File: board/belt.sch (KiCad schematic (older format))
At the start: 21 parts, among them J1 USB_B_Micro, J2 USB_B_Micro, J3 USB_B_Micro, J4 USB_B_Micro, Q1 BSS138, Q2 BSS138, SW1 SW_SPST, SW2 SW_Push, U1 Teensy4.0, U2 Adafruit_BNO055

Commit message: first pass at pcb layout; also start looking into adding an NPN switch so that LED current doesn't have to travel through the rest of the board (concerns about wire thickness, heat, etc.)
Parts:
- added Q3: TIP120, Package_TO_SOT_THT:TO-220-3_Vertical, symbol Transistor_BJT:TIP120
- added R5: 5K, Resistor_SMD:R_0805_2012Metric, symbol Device:R_Small_US
- MK1: symbol SPW2430HR5H-B:SPW2430HR5H-B -> MIC_SPW2430HR5H-B:SPW2430HR5H-B
- R5: symbol 3352T-1-103LF:3352T-1-103LF -> belt-rescue:3352T-1-103LF-3352T-1-103LF
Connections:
- net labels added: GND_SWITCH
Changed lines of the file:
@@
-	1    0    0    -1
-$EndComp
-$Comp
-L power:GND #PWR0116
-U 1 1 5E3355B9
-P 4000 5700
-F 0 "#PWR0116" H 4000 5450 50  0001 C CNN
-F 1 "GND" V 4005 5572 50  0000 R CNN
-F 2 "" H 4000 5700 50  0001 C CNN
-F 3 "" H 4000 5700 50  0001 C CNN
-	1    4000 5700
 	1    0    0    -1
 $EndComp
 Connection ~ 3000 5600
-Wire Wire Line
-	2700 5600 3000 5600
 $Comp
 L Device:C C1
@@
 	3450 7150 3450 6950
 $Comp
-L SPW2430HR5H-B:SPW2430HR5H-B MK1
+L MIC_SPW2430HR5H-B:SPW2430HR5H-B MK1
 U 1 1 5E34E597
 P 3250 6450
@@
 BUTTON
 $Comp
-L 3352T-1-103LF:3352T-1-103LF R5
+L belt-rescue:3352T-1-103LF-3352T-1-103LF R5
 U 1 1 5E3B3B17
 P 1500 1050
@@
 	0    1    1    0
 $EndComp
-$Comp
-L power:VDD #PWR0123
-U 1 1 5E3B5DE6
-P 1800 1050
-F 0 "#PWR0123" H 1800 900 50  0001 C CNN
-F 1 "VDD" V 1817 1178 50  0000 L CNN
-F 2 "" H 1800 1050 50  0001 C CNN
-F 3 "" H 1800 1050 50  0001 C CNN
-	1    1800 1050
-	0    1    1    0
-$EndComp
 Text Label 6650 950  1    50   ~ 0
 THUMBDIAL
@@
 Text Label 6450 3150 3    50   ~ 0
 MOTION_SCL
-$Comp
-L power:GND #PWR0112
-U 1 1 5E31B962
-P 4000 4500
-F 0 "#PWR0112" H 4000 4250 50  0001 C CNN
-F 1 "GND" V 4005 4372 50  0000 R CNN
-F 2 "" H 4000 4500 50  0001 C CNN
-F 3 "" H 4000 4500 50  0001 C CNN
-	1    4000 4500
-	1    0    0    -1
-$EndComp
 $Comp
 L power:VDD #PWR02
@@
 Connection ~ 3650 5600
 $Comp
-L power:GND #PWR0129
-U 1 1 5E37E624
-P 4300 4900
-F 0 "#PWR0129" H 4300 4650 50  0001 C CNN
-F 1 "GND" V 4305 4772 50  0000 R CNN
-F 2 "" H 4300 4900 50  0001 C CNN
-F 3 "" H 4300 4900 50  0001 C CNN
-	1    4300 4900
-	0    1    1    0
-$EndComp
-$Comp
 L power:VDD #PWR0130
 U 1 1 5E37EDC1
@@
 $EndComp
 $Comp
-L power:GND #PWR0131
-U 1 1 5E3831AA
-P 4300 6100
-F 0 "#PWR0131" H 4300 5850 50  0001 C CNN
-F 1 "GND" V 4305 5972 50  0000 R CNN
-F 2 "" H 4300 6100 50  0001 C CNN
-F 3 "" H 4300 6100 50  0001 C CNN
-	1    4300 6100
-	0    1    1    0
-$EndComp
-$Comp
 L power:VDD #PWR0132
 U 1 1 5E3831B0
@@
 NoConn ~ 2750 1200
 NoConn ~ 2850 1200
+$Comp
+L power:+3.3V #PWR0123
+U 1 1 5E3638F7
+P 1800 1050
+F 0 "#PWR0123" H 1800 900 50  0001 C CNN
+F 1 "+3.3V" V 1815 1178 50  0000 L CNN
+F 2 "" H 1800 1050 50  0001 C CNN
+F 3 "" H 1800 1050 50  0001 C CNN
+	1    1800 1050
+	0    1    1    0
+$EndComp
+Wire Wire Line
+	2700 5600 3000 5600
+Text Label 2850 3250 0    50   ~ 0
+GND_SWITCH
+Text Label 4300 6100 2    50   ~ 0
+GND_SWITCH
+Text Label 4000 5700 2    50   ~ 0
+GND_SWITCH
+Text Label 4300 4900 2    50   ~ 0
+GND_SWITCH
+Text Label 4000 4500 2    50   ~ 0
+GND_SWITCH
+$Comp
+L Transistor_BJT:TIP120 Q3
+U 1 1 5E42DE1B
+P 2650 3150
+F 0 "Q3" V 2901 3150 50  0000 C CNN
+F 1 "TIP120" V 2992 3150 50  0000 C CNN
+F 2 "Package_TO_SOT_THT:TO-220-3_Vertical" H 2850 3075 50  0001 L CIN
+F 3 "http://www.fairchildsemi.com/ds/TI/TIP120.pdf" H 2650 3150 50  0001 L CNN
+	1    2650 3150
+	0    1    1    0
+$EndComp
+$Comp
+L power:GND #PWR?
+U 1 1 5E433994
+P 2450 3250
+F 0 "#PWR?" H 2450 3000 50  0001 C CNN
+F 1 "GND" V 2455 3122 50  0000 R CNN
+F 2 "" H 2450 3250 50  0001 C CNN
+F 3 "" H 2450 3250 50  0001 C CNN
+	1    2450 3250
+	0    1    1    0
+$EndComp
+$Comp
+L power:VDD #PWR?
+U 1 1 5E434E74
+P 2650 2750
+F 0 "#PWR?" H 2650 2600 50  0001 C CNN
+F 1 "VDD" V 2667 2878 50  0000 L CNN
+F 2 "" H 2650 2750 50  0001 C CNN
+F 3 "" H 2650 2750 50  0001 C CNN
+	1    2650 2750
+	1    0    0    -1
+$EndComp
+$Comp
+L Device:R_Small_US R5
+U 1 1 5E43706E
+P 2650 2850
+F 0 "R5" H 2718 2896 50  0000 L CNN
+F 1 "5K" H 2718 2805 50  0000 L CNN
+F 2 "Resistor_SMD:R_0805_2012Metric" H 2650 2850 50  0001 C CNN
+F 3 "~" H 2650 2850 50  0001 C CNN
+	1    2650 2850
+	1    0    0    -1
+$EndComp
 $EndSCHEMATC

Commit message: alternate layout with thick wires and switch on top to avoid needing a transistor to switch power nearby (would likely need a large transistor with a heatsink to manage the current)
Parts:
- removed Q3: TIP120, Package_TO_SOT_THT:TO-220-3_Vertical, symbol Transistor_BJT:TIP120
- removed R5: 5K, Resistor_SMD:R_0805_2012Metric, symbol Device:R_Small_US
- renumbered R5 to P1
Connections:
- net labels added: MIC_PWR
- net labels removed: GND_SWITCH
- no-connect marks 64 -> 63
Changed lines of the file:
@@
-	0    1    1    0
-$EndComp
-$Comp
-L power:+3.3V #PWR0114
-U 1 1 5E354D35
-P 3600 7150
-F 0 "#PWR0114" H 3600 7000 50  0001 C CNN
-F 1 "+3.3V" V 3615 7278 50  0000 L CNN
-F 2 "" H 3600 7150 50  0001 C CNN
-F 3 "" H 3600 7150 50  0001 C CNN
-	1    3600 7150
 	0    1    1    0
 $EndComp
@@
 Text Label 2700 5600 2    50   ~ 0
 DATA2
-NoConn ~ 6450 950
 $Comp
 L power:VDD #PWR0117
@@
 $EndComp
 $Comp
-L power:VDD #PWR0120
-U 1 1 5E3ACFA6
-P 1700 2200
-F 0 "#PWR0120" H 1700 2050 50  0001 C CNN
-F 1 "VDD" V 1717 2328 50  0000 L CNN
-F 2 "" H 1700 2200 50  0001 C CNN
-F 3 "" H 1700 2200 50  0001 C CNN
-	1    1700 2200
-	0    1    1    0
-$EndComp
-$Comp
 L Switch:SW_Push SW2
 U 1 1 5E3ADC97
@@
 BUTTON
 $Comp
-L belt-rescue:3352T-1-103LF-3352T-1-103LF R5
+L belt-rescue:3352T-1-103LF-3352T-1-103LF P1
 U 1 1 5E3B3B17
 P 1500 1050
-F 0 "R5" H 1500 1165 50  0000 C CNN
+F 0 "P1" H 1500 1165 50  0000 C CNN
 F 1 "3352T-1-103LF" H 1500 1256 50  0000 C CNN
 F 2 "3352T-1-103LF:TRIM_3352T-1-103LF" H 1500 1050 50  0001 L BNN
@@
 Wire Wire Line
 	1450 5150 1750 5150
-$Comp
-L power:VBUS #PWR0111
-U 1 1 5E3E2BC8
-P 1300 2200
-F 0 "#PWR0111" H 1300 2050 50  0001 C CNN
-F 1 "VBUS" V 1315 2328 50  0000 L CNN
-F 2 "" H 1300 2200 50  0001 C CNN
-F 3 "" H 1300 2200 50  0001 C CNN
-	1    1300 2200
-	0    -1   -1   0
-$EndComp
 Wire Wire Line
 	1450 4250 1750 4250
@@
 Wire Wire Line
 	2700 5600 3000 5600
-Text Label 2850 3250 0    50   ~ 0
-GND_SWITCH
-Text Label 4300 6100 2    50   ~ 0
-GND_SWITCH
-Text Label 4000 5700 2    50   ~ 0
-GND_SWITCH
-Text Label 4300 4900 2    50   ~ 0
-GND_SWITCH
-Text Label 4000 4500 2    50   ~ 0
-GND_SWITCH
-$Comp
-L Transistor_BJT:TIP120 Q3
-U 1 1 5E42DE1B
-P 2650 3150
-F 0 "Q3" V 2901 3150 50  0000 C CNN
-F 1 "TIP120" V 2992 3150 50  0000 C CNN
-F 2 "Package_TO_SOT_THT:TO-220-3_Vertical" H 2850 3075 50  0001 L CIN
-F 3 "http://www.fairchildsemi.com/ds/TI/TIP120.pdf" H 2650 3150 50  0001 L CNN
-	1    2650 3150
-	0    1    1    0
-$EndComp
-$Comp
-L power:GND #PWR?
-U 1 1 5E433994
-P 2450 3250
-F 0 "#PWR?" H 2450 3000 50  0001 C CNN
-F 1 "GND" V 2455 3122 50  0000 R CNN
-F 2 "" H 2450 3250 50  0001 C CNN
-F 3 "" H 2450 3250 50  0001 C CNN
-	1    2450 3250
-	0    1    1    0
-$EndComp
-$Comp
-L power:VDD #PWR?
-U 1 1 5E434E74
-P 2650 2750
-F 0 "#PWR?" H 2650 2600 50  0001 C CNN
-F 1 "VDD" V 2667 2878 50  0000 L CNN
-F 2 "" H 2650 2750 50  0001 C CNN
-F 3 "" H 2650 2750 50  0001 C CNN
-	1    2650 2750
-	1    0    0    -1
-$EndComp
-$Comp
-L Device:R_Small_US R5
-U 1 1 5E43706E
-P 2650 2850
-F 0 "R5" H 2718 2896 50  0000 L CNN
-F 1 "5K" H 2718 2805 50  0000 L CNN
-F 2 "Resistor_SMD:R_0805_2012Metric" H 2650 2850 50  0001 C CNN
-F 3 "~" H 2650 2850 50  0001 C CNN
-	1    2650 2850
-	1    0    0    -1
-$EndComp
+$Comp
+L power:VDD #PWR0120
+U 1 1 5E3ACFA6
+P 1300 2200
+F 0 "#PWR0120" H 1300 2050 50  0001 C CNN
+F 1 "VDD" V 1317 2328 50  0000 L CNN
+F 2 "" H 1300 2200 50  0001 C CNN
+F 3 "" H 1300 2200 50  0001 C CNN
+	1    1300 2200
+	0    -1   -1   0
+$EndComp
+$Comp
+L power:VBUS #PWR0111
+U 1 1 5E3E2BC8
+P 1700 2200
+F 0 "#PWR0111" H 1700 2050 50  0001 C CNN
+F 1 "VBUS" V 1715 2328 50  0000 L CNN
+F 2 "" H 1700 2200 50  0001 C CNN
+F 3 "" H 1700 2200 50  0001 C CNN
+	1    1700 2200
+	0    1    1    0
+$EndComp
+$Comp
+L power:GND #PWR0112
+U 1 1 5E49DFB8
+P 4000 4500
+F 0 "#PWR0112" H 4000 4250 50  0001 C CNN
+F 1 "GND" H 4005 4327 50  0000 C CNN
+F 2 "" H 4000 4500 50  0001 C CNN
+F 3 "" H 4000 4500 50  0001 C CNN
+	1    4000 4500
+	1    0    0    -1
+$EndComp
+$Comp
+L power:GND #PWR0116
+U 1 1 5E49E6CA
+P 4000 5700
+F 0 "#PWR0116" H 4000 5450 50  0001 C CNN
+F 1 "GND" H 4005 5527 50  0000 C CNN
+F 2 "" H 4000 5700 50  0001 C CNN
+F 3 "" H 4000 5700 50  0001 C CNN
+	1    4000 5700
+	1    0    0    -1
+$EndComp
+$Comp
+L power:GND #PWR0129
+U 1 1 5E49EE23
+P 4300 6100
+F 0 "#PWR0129" H 4300 5850 50  0001 C CNN
+F 1 "GND" V 4305 5972 50  0000 R CNN
+F 2 "" H 4300 6100 50  0001 C CNN
+F 3 "" H 4300 6100 50  0001 C CNN
+	1    4300 6100
+	0    1    1    0
+$EndComp
+$Comp
+L power:GND #PWR0131
+U 1 1 5E4A05FE
+P 4300 4900
+F 0 "#PWR0131" H 4300 4650 50  0001 C CNN
+F 1 "GND" V 4305 4772 50  0000 R CNN
+F 2 "" H 4300 4900 50  0001 C CNN
+F 3 "" H 4300 4900 50  0001 C CNN
+	1    4300 4900
+	0    1    1    0
+$EndComp
+Text Label 6450 950  1    50   ~ 0
+MIC_PWR
+Text Label 3600 7150 0    50   ~ 0
+MIC_PWR
 $EndSCHEMATC

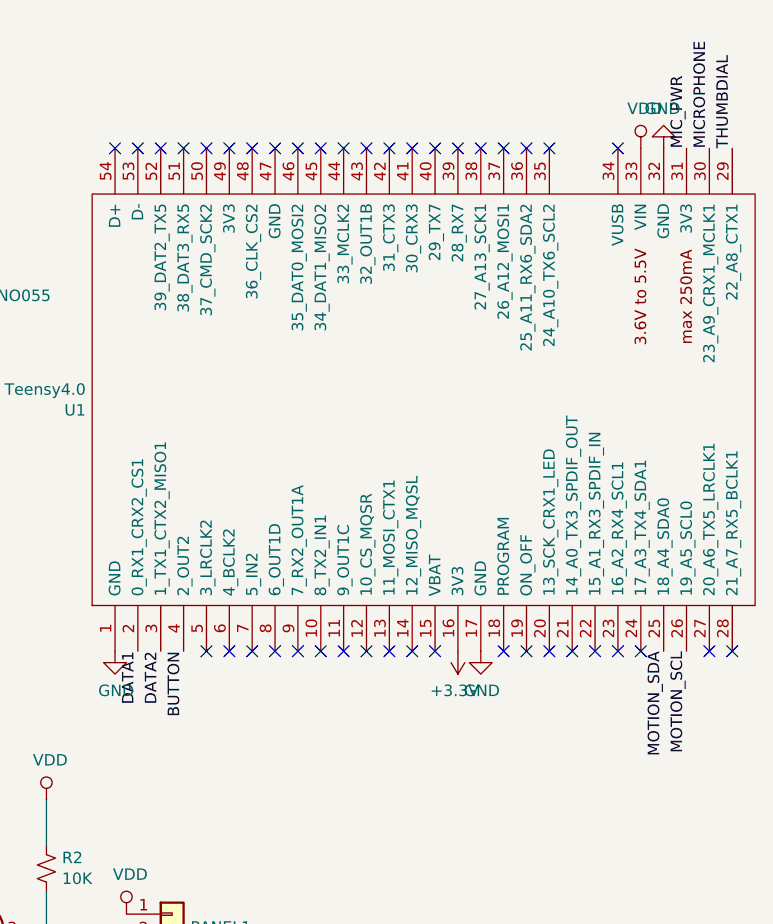
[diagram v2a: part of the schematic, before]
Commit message: move pot and button ports to be nearer by on teensy
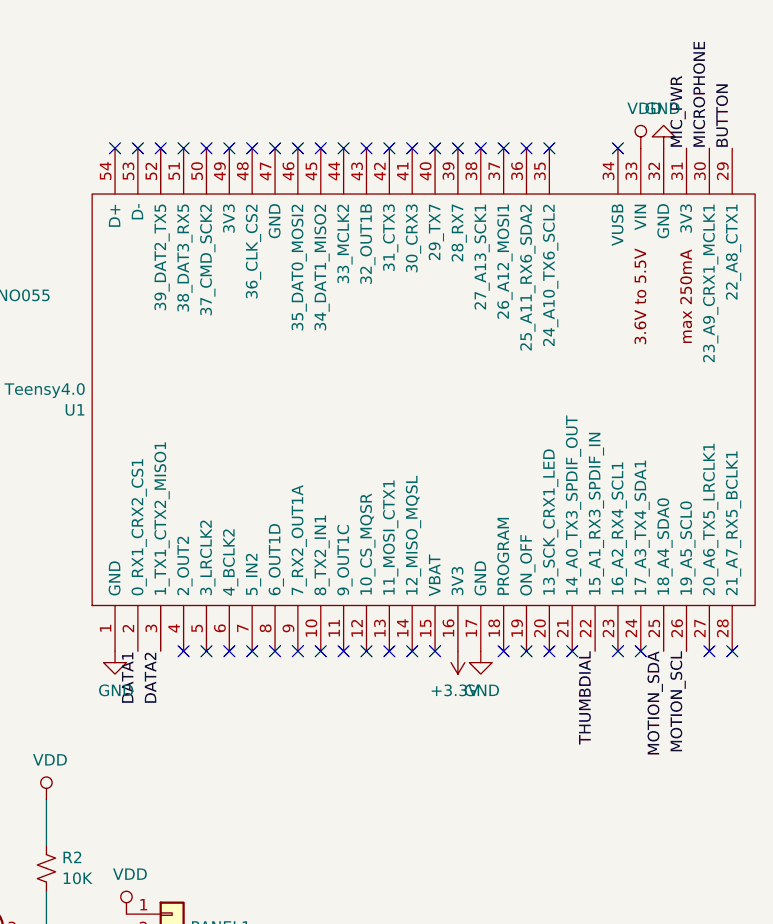
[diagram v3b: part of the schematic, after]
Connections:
- net BUTTON: now also U1.29 (22_A8_CTX1); no longer U1.4 (2_OUT2)
- net THUMBDIAL: now also U1.22 (15_A1_RX3_SPDIF_IN); no longer U1.29 (22_A8_CTX1)
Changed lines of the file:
@@
 	0    1    1    0
 $EndComp
-Text Label 6550 950  1    50   ~ 0
-MICROPHONE
 Text Label 4050 3150 3    50   ~ 0
 DATA1
@@
 Text Label 1700 1750 0    50   ~ 0
 BUTTON
-Text Label 4250 3150 3    50   ~ 0
+Text Label 6650 950  1    50   ~ 0
 BUTTON
 $Comp
@@
 	0    1    1    0
 $EndComp
-Text Label 6650 950  1    50   ~ 0
+Text Label 6050 3150 3    50   ~ 0
 THUMBDIAL
 Text Label 1500 850  0    50   ~ 0
@@
 NoConn ~ 6250 3150
 NoConn ~ 6150 3150
-NoConn ~ 6050 3150
 NoConn ~ 5950 3150
 NoConn ~ 5850 3150
@@
 Text Label 3600 7150 0    50   ~ 0
 MIC_PWR
+Text Label 6550 950  1    50   ~ 0
+MICROPHONE
+NoConn ~ 4250 3150
 $EndSCHEMATC

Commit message: mostly done with next board iteration, except for new microphone; use new microphone in software to draw a rainbow fft that is super fun to play with
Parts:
- P1: footprint 3352T-1-103LF:TRIM_3352T-1-103LF -> Potentiometer_THT:PDB12-H
- SW1: value SW_SPST -> SW_DPDT; footprint Button_Switch_SMD:SW_SPDT_PCM12 -> engstad:slide-switch-MFS201N-9-Z; symbol Switch:SW_SPST -> Switch:SW_DPDT_x2
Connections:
- net +3V3: now also C1.1, MK1.4 (VDD)
- net BUTTON: now also U1.24 (17_A3_TX4_SDA1); no longer U1.29 (22_A8_CTX1)
- net MICROPHONE: now also U1.21 (14_A0_TX3_SPDIF_OUT); no longer U1.30 (23_A9_CRX1_MCLK1)
- net VBUS: now also SW1.1 (A); no longer SW1.2 (B)
- net VDD: now also SW1.2 (B); no longer SW1.1 (A)
- removed net MIC_PWR: C1.1, MK1.4 (VDD), U1.31 (3V3)
- no-connect marks 63 -> 65
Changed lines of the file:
@@
 $EndComp
 $Comp
-L Switch:SW_SPST SW1
+L Switch:SW_DPDT_x2 SW1
 U 1 1 5E3A9D22
 P 1500 2200
 F 0 "SW1" H 1500 2435 50  0000 C CNN
-F 1 "SW_SPST" H 1500 2344 50  0000 C CNN
-F 2 "Button_Switch_SMD:SW_SPDT_PCM12" H 1500 2200 50  0001 C CNN
+F 1 "SW_DPDT" H 1500 2344 50  0000 C CNN
+F 2 "engstad:slide-switch-MFS201N-9-Z" H 1500 2200 50  0001 C CNN
 F 3 "~" H 1500 2200 50  0001 C CNN
 	1    1500 2200
@@
 Text Label 1700 1750 0    50   ~ 0
 BUTTON
-Text Label 6650 950  1    50   ~ 0
+Text Label 6250 3150 3    50   ~ 0
 BUTTON
 $Comp
@@
 F 0 "P1" H 1500 1165 50  0000 C CNN
 F 1 "3352T-1-103LF" H 1500 1256 50  0000 C CNN
-F 2 "3352T-1-103LF:TRIM_3352T-1-103LF" H 1500 1050 50  0001 L BNN
+F 2 "Potentiometer_THT:PDB12-H" H 1500 1050 50  0001 L BNN
 F 3 "" H 1500 1050 50  0001 L BNN
 F 4 "IPC-7351B" H 1500 1050 50  0001 L BNN "Field4"
@@
 NoConn ~ 6650 3150
 NoConn ~ 6550 3150
-NoConn ~ 6250 3150
+NoConn ~ 6650 950
 NoConn ~ 6150 3150
-NoConn ~ 5950 3150
+NoConn ~ 6550 950
 NoConn ~ 5850 3150
 NoConn ~ 5750 3150
@@
 L power:VBUS #PWR0111
 U 1 1 5E3E2BC8
-P 1700 2200
-F 0 "#PWR0111" H 1700 2050 50  0001 C CNN
-F 1 "VBUS" V 1715 2328 50  0000 L CNN
-F 2 "" H 1700 2200 50  0001 C CNN
-F 3 "" H 1700 2200 50  0001 C CNN
-	1    1700 2200
+P 1700 2100
+F 0 "#PWR0111" H 1700 1950 50  0001 C CNN
+F 1 "VBUS" V 1715 2228 50  0000 L CNN
+F 2 "" H 1700 2100 50  0001 C CNN
+F 3 "" H 1700 2100 50  0001 C CNN
+	1    1700 2100
 	0    1    1    0
 $EndComp
@@
 	0    1    1    0
 $EndComp
-Text Label 6450 950  1    50   ~ 0
-MIC_PWR
-Text Label 3600 7150 0    50   ~ 0
-MIC_PWR
-Text Label 6550 950  1    50   ~ 0
+Text Label 5950 3150 3    50   ~ 0
 MICROPHONE
 NoConn ~ 4250 3150
+NoConn ~ 1700 2300
+NoConn ~ 6450 950
+$Comp
+L power:+3.3V #PWR0114
+U 1 1 5E49B29A
+P 3600 7150
+F 0 "#PWR0114" H 3600 7000 50  0001 C CNN
+F 1 "+3.3V" V 3615 7278 50  0000 L CNN
+F 2 "" H 3600 7150 50  0001 C CNN
+F 3 "" H 3600 7150 50  0001 C CNN
+	1    3600 7150
+	0    1    1    0
+$EndComp
 $EndSCHEMATC
